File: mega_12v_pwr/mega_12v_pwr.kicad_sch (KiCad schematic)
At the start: 67 parts, among them J1 Conn_01x01, J10 Conn_01x01, J11 Conn_01x01, J12 Conn_01x01, J13 Conn_01x01, J14 Conn_01x01, J15 Conn_01x01, J16 Conn_01x01, J17 Conn_01x01, J18 Conn_01x01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

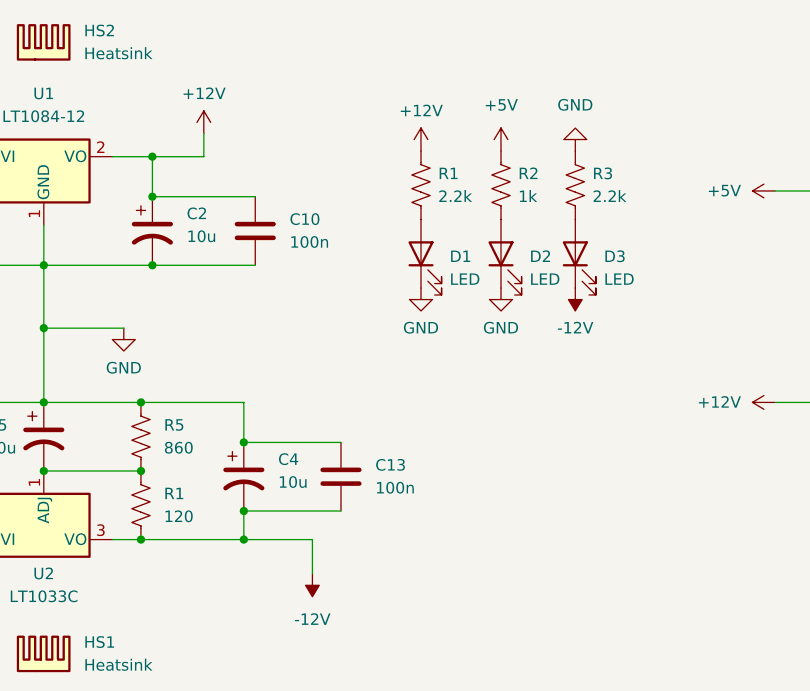
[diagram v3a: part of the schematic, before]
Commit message: Updated resistor values
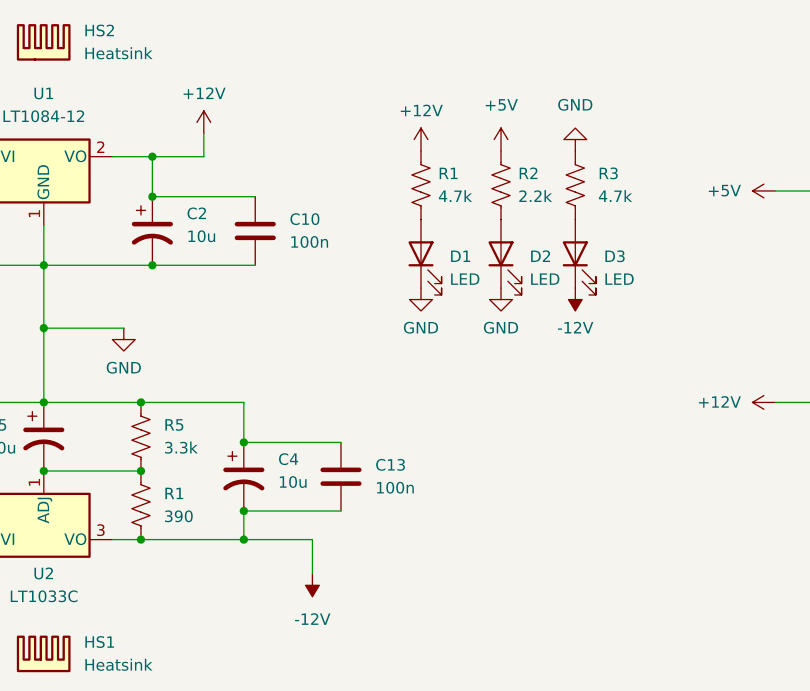
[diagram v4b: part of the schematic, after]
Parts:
- R1, R3: value 2.2k -> 4.7k
- R1: value 120 -> 390
- R2: value 1k -> 2.2k
- R5: value 860 -> 3.3k
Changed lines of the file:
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@@
       (effects (font (size 1.27 1.27)) (justify left))
     )
-    (property "Value" "860" (at 147.32 78.74 0)
+    (property "Value" "3.3k" (at 147.32 78.74 0)
       (effects (font (size 1.27 1.27)) (justify left))
     )
@@
       (effects (font (size 1.27 1.27)) (justify left))
     )
-    (property "Value" "1k" (at 186.69 50.8 0)
+    (property "Value" "2.2k" (at 186.69 50.8 0)
       (effects (font (size 1.27 1.27)) (justify left))
     )
@@
       (effects (font (size 1.27 1.27)) (justify left))
     )
-    (property "Value" "2.2k" (at 177.8 50.8 0)
+    (property "Value" "4.7k" (at 177.8 50.8 0)
       (effects (font (size 1.27 1.27)) (justify left))
     )
@@
       (effects (font (size 1.27 1.27)) (justify left))
     )
-    (property "Value" "120" (at 147.32 86.36 0)
+    (property "Value" "390" (at 147.32 86.36 0)
       (effects (font (size 1.27 1.27)) (justify left))
     )
@@
   (symbol (lib_id "Device:R_US") (at 193.04 49.53 0) (unit 1)
     (in_bom yes) (on_board yes) (dnp no) (fields_autoplaced)
-    (property "Reference" "R3" (at 194.945 48.26 0)
-      (effects (font (size 1.27 1.27)) (justify left))
-    )
-    (property "Value" "2.2k" (at 194.945 50.8 0)
-      (effects (font (size 1.27 1.27)) (justify left))
-    )
+    (property "Reference" "R3" (at 195.58 48.26 0)
+      (effects (font (size 1.27 1.27)) (justify left))
+    )
+    (property "Value" "4.7k" (at 195.58 50.8 0)
+      (effects (font (size 1.27 1.27)) (justify left))
+    )
